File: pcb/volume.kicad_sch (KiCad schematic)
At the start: 0 parts

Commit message: WIP PCB
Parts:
- added C? (x4): 1μF, symbol Device:C_Polarized
- added C? (x4): 75pF, symbol Device:C
- added R? (x16): 4.7kΩ, symbol Device:R
- added U? (x4): 74LS573, symbol 74xx:74LS573
- added U? (x5): TL074, symbol Amplifier_Operational:TL074
- added U? (x4): DAC0808_DIP, Package_DIP:DIP-16_W7.62mm, symbol Analog_DAC:DAC0808_DIP
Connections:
- new net: U?.12 (A1), U?.12 (Q7) (x4)
- new net: U?.11 (A2), U?.13 (Q6) (x4)
- new net: U?.10 (A3), U?.14 (Q5) (x4)
- new net: U?.15 (Q4), U?.9 (A4) (x4)
- new net: U?.16 (Q3), U?.8 (A5) (x4)
- new net: U?.17 (Q2), U?.7 (A6) (x4)
- new net: U?.18 (Q1), U?.6 (A7) (x4)
- new net: U?.19 (Q0), U?.5 (A8) (x4)
- new net: C?.1, R?.2, U?.8
- new net: R?.1, U?.4 (I0), U?.9 (-)
- new net: C?.1, R?.2, U?.7
- new net: R?.1, U?.4 (I0), U?.6 (-)
- new net: R?.1, U?.15 (VREF-) (x4)
- new net: C?.1, R?.2, U?.1
- new net: R?.1, U?.2 (-), U?.4 (I0)
- new net: R?.1, U?.14 (VREF+) (x4)
- new net: C?.1, U?.16 (COMPEN) (x4)
- new net: R?.1, U?.13 (-), U?.4 (I0)
- new net: C?.1, R?.2, U?.14
- new net +5V: U?.20 (VCC), U?.20 (VCC), U?.20 (VCC), U?.20 (VCC)
- new net +5VA: R?.2, R?.2, R?.2, R?.2
- new net +9VA: U?.13 (VCC), U?.13 (VCC), U?.13 (VCC), U?.13 (VCC), U?.4 (V+)
- new net -9VA: C?.2, C?.2, C?.2, C?.2, U?.11 (V-), U?.3 (VEE), U?.3 (VEE), U?.3 (VEE), U?.3 (VEE)
- new net D0: U?.2 (D0), U?.2 (D0), U?.2 (D0), U?.2 (D0)
- new net D1: U?.3 (D1), U?.3 (D1), U?.3 (D1), U?.3 (D1)
- new net D2: U?.4 (D2), U?.4 (D2), U?.4 (D2), U?.4 (D2)
- new net D3: U?.5 (D3), U?.5 (D3), U?.5 (D3), U?.5 (D3)
- new net D4: U?.6 (D4), U?.6 (D4), U?.6 (D4), U?.6 (D4)
- new net D5: U?.7 (D5), U?.7 (D5), U?.7 (D5), U?.7 (D5)
- new net D6: U?.8 (D6), U?.8 (D6), U?.8 (D6), U?.8 (D6)
- new net D7: U?.9 (D7), U?.9 (D7), U?.9 (D7), U?.9 (D7)
- new net GND: U?.1 (OE), U?.1 (OE), U?.1 (OE), U?.1 (OE), U?.10 (GND), U?.10 (GND), U?.10 (GND), U?.10 (GND)
- new net GNDA: R?.2, R?.2, R?.2, R?.2, U?.10 (+), U?.12 (+), U?.2 (GND), U?.2 (GND), U?.2 (GND), U?.2 (GND), U?.3 (+), U?.5 (+)
- new net IN0: R?.2
- new net IN1: R?.2
- new net IN2: R?.2
- new net IN3: R?.2
- new net LOAD0: U?.11 (Load)
- new net LOAD1: U?.11 (Load)
- new net LOAD2: U?.11 (Load)
- new net LOAD3: U?.11 (Load)
- new net OUT0: C?.2, R?.1
- new net OUT1: C?.2, R?.1
- new net OUT2: C?.2, R?.1
- new net OUT3: C?.2, R?.1

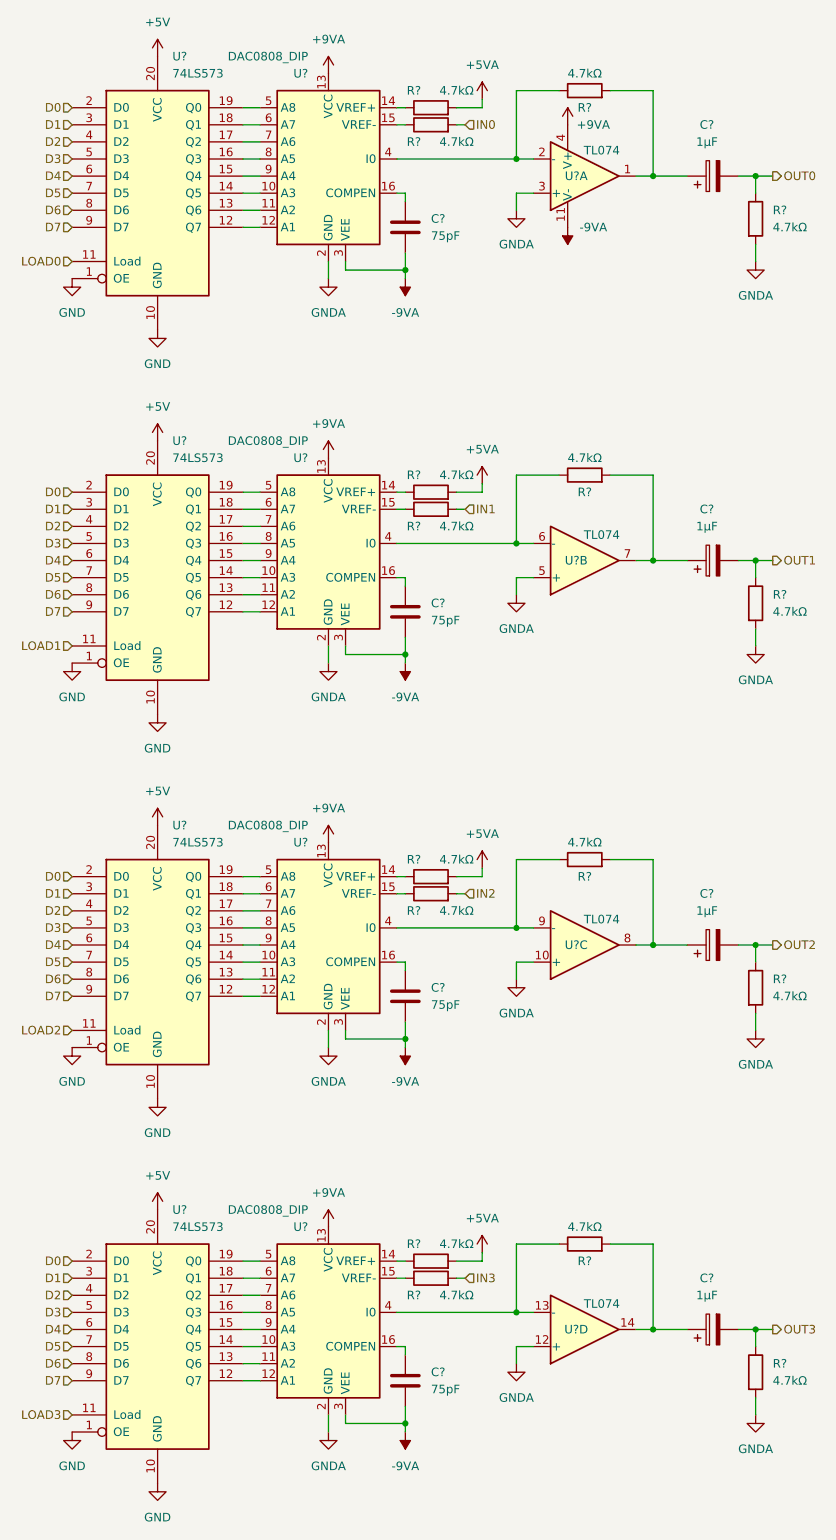
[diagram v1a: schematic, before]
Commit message: PCB: add reset circuit, xtal
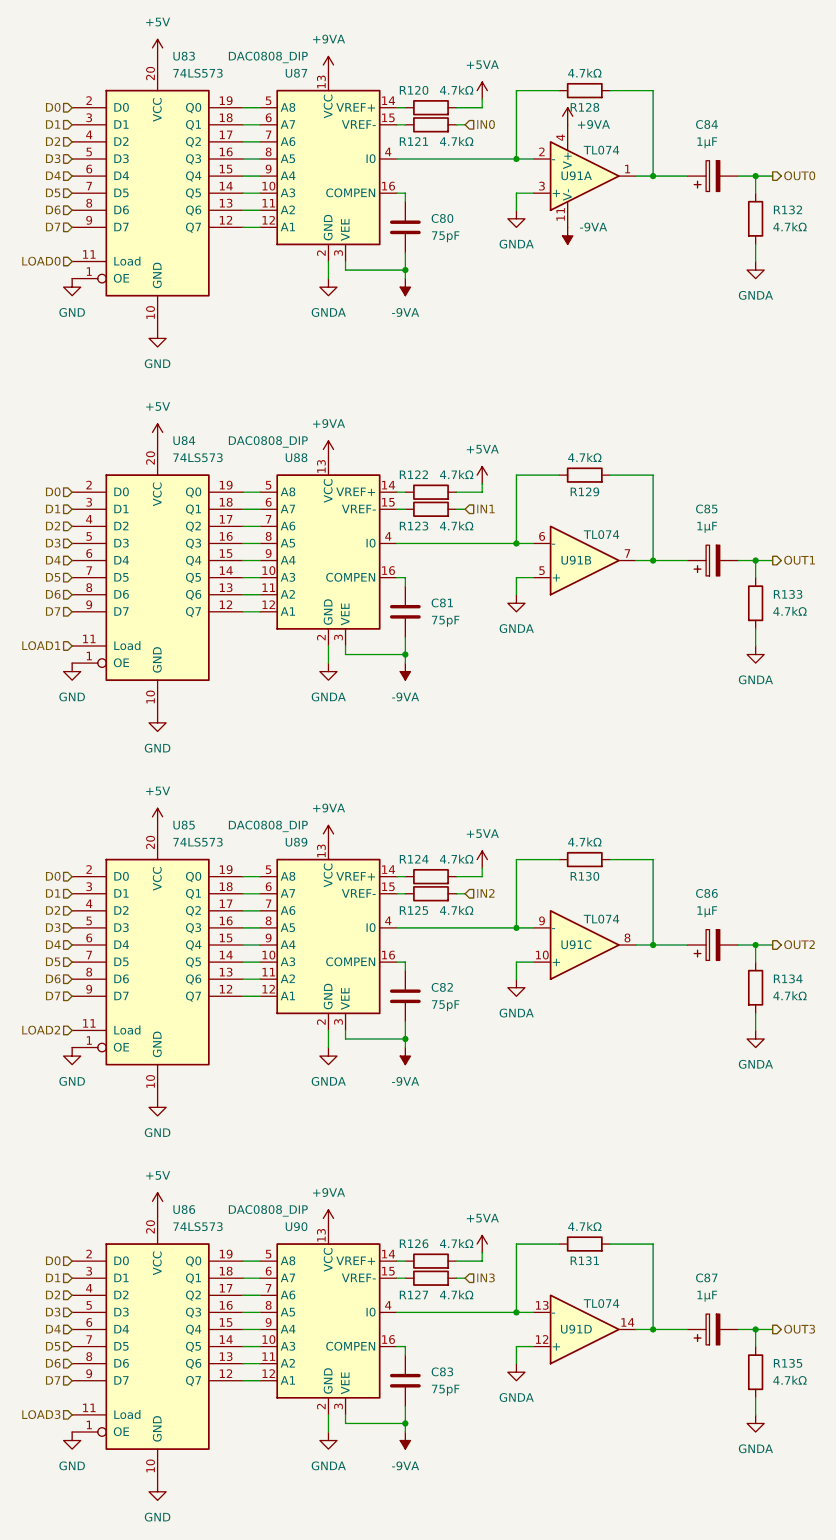
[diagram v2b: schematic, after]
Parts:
- gave numbers to parts that had none: 33

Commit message: WIP schematic
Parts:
- renumbered C80 to C84, C81 to C85, C82 to C86, C83 to C87, C84 to C88, C85 to C89, C86 to C90, C87 to C91, R120 to R127, R121 to R128, R122 to R129, R123 to R130, R124 to R131, R125 to R132, R126 to R133, R127 to R134, R128 to R135, R129 to R136, R130 to R137, R131 to R138, R132 to R139, R133 to R140, R134 to R141, R135 to R142, U83 to U84, U84 to U85, U85 to U86, U86 to U87, U87 to U88, U88 to U89, U89 to U90, U90 to U91, U91 to U92

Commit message: WIP schematic
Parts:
- removed C88, C89, C90, C91: 1μF, symbol Device:C_Polarized
- added C101, C102, C103, C104: 1µF, symbol Device:C
- renumbered C87 to C100, C84 to C97, C85 to C98, C86 to C99, R127 to R153, R128 to R154, R129 to R155, R130 to R156, R131 to R157, R132 to R158, R133 to R159, R134 to R160, R135 to R161, R136 to R162, R137 to R163, R138 to R164, R139 to R165, R140 to R166, R141 to R167, R142 to R168, U84 to U85, U85 to U86, U86 to U87, U87 to U88, U88 to U89, U89 to U90, U90 to U91, U91 to U92, U92 to U93
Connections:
- net OUT0: now also C101.2
- net OUT1: now also C102.2
- net OUT2: now also C103.2
- net OUT3: now also C104.2
- net at R163.2, U93.8: now also C103.1
- net at R162.2, U93.7: now also C102.1
- net at R161.2, U93.1: now also C101.1
- net at R164.2, U93.14: now also C104.1

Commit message: WIP schematic
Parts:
- renumbered C97 to C102, C98 to C103, C99 to C104, C100 to C105, C101 to C106, C102 to C107, C103 to C108, C104 to C109

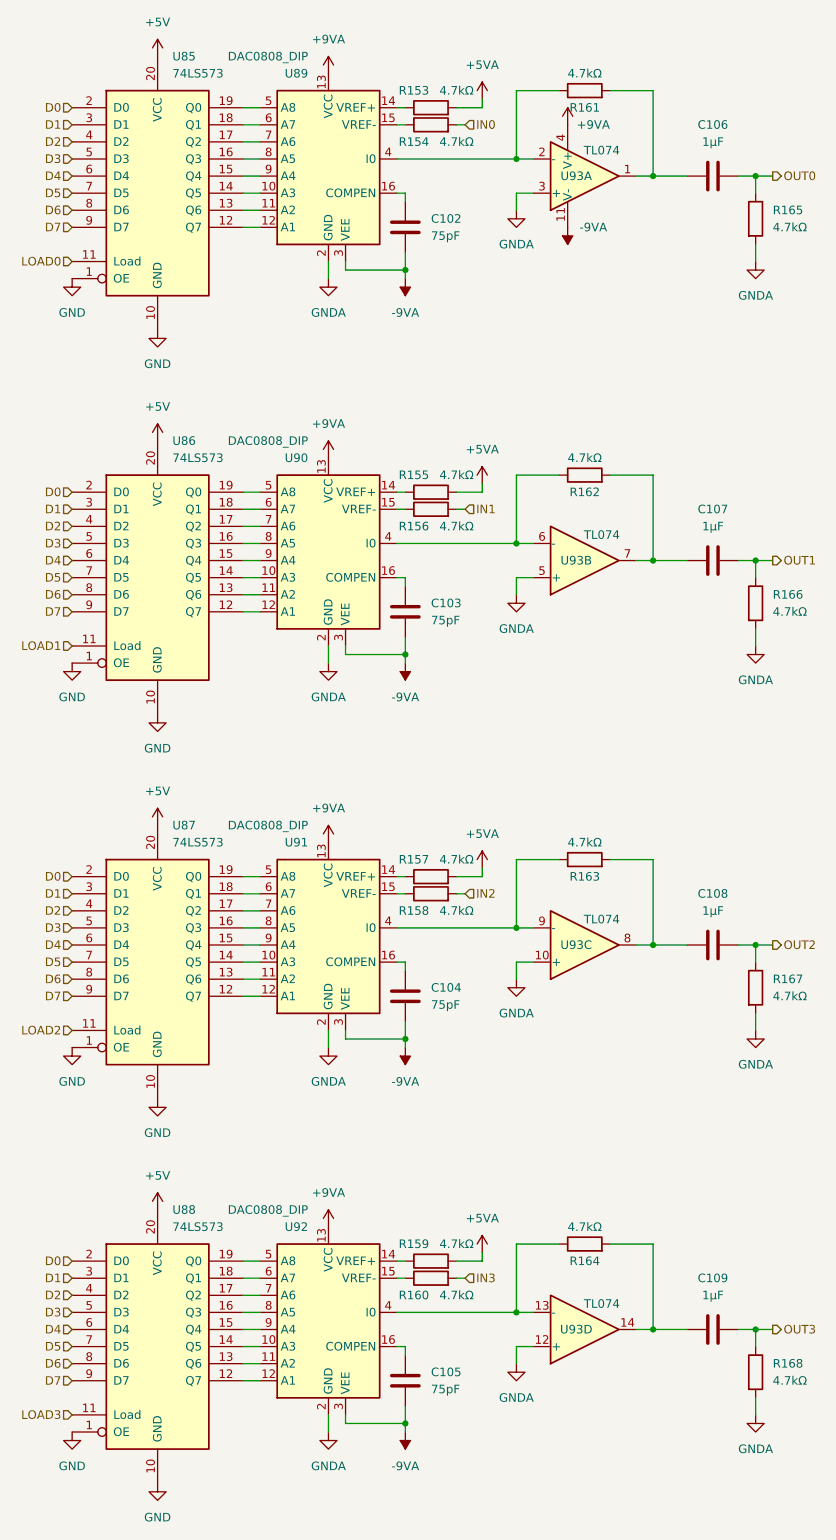
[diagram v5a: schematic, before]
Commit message: WIP PCB (add bypass caps, minor fixes)
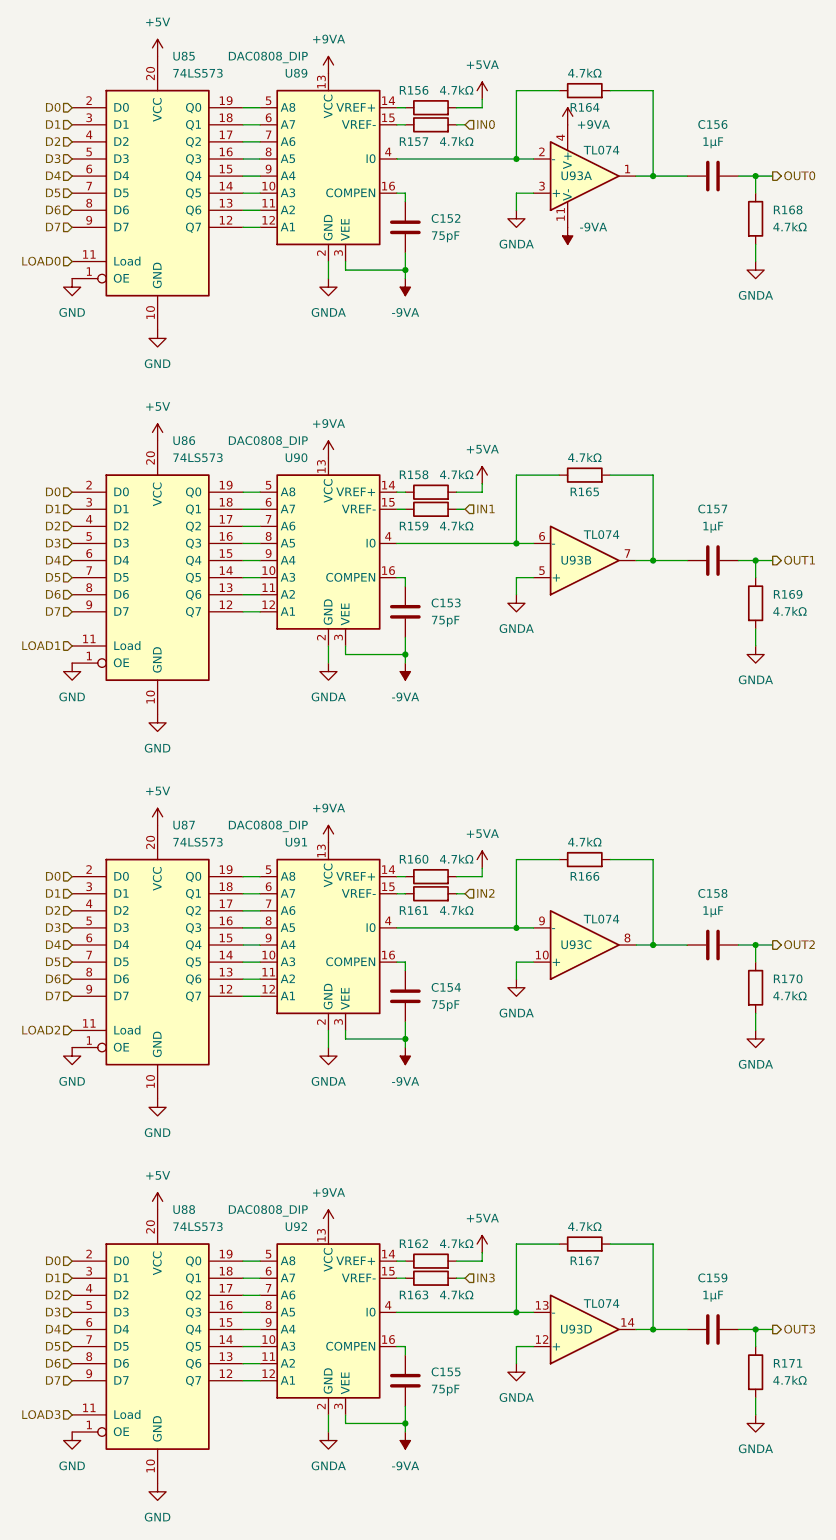
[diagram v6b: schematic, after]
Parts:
- renumbered C102 to C152, C103 to C153, C104 to C154, C105 to C155, C106 to C156, C107 to C157, C108 to C158, C109 to C159, R153 to R156, R154 to R157, R155 to R158, R156 to R159, R157 to R160, R158 to R161, R159 to R162, R160 to R163, R161 to R164, R162 to R165, R163 to R166, R164 to R167, R165 to R168, R166 to R169, R167 to R170, R168 to R171
